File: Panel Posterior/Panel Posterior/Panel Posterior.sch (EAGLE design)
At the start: 1 part

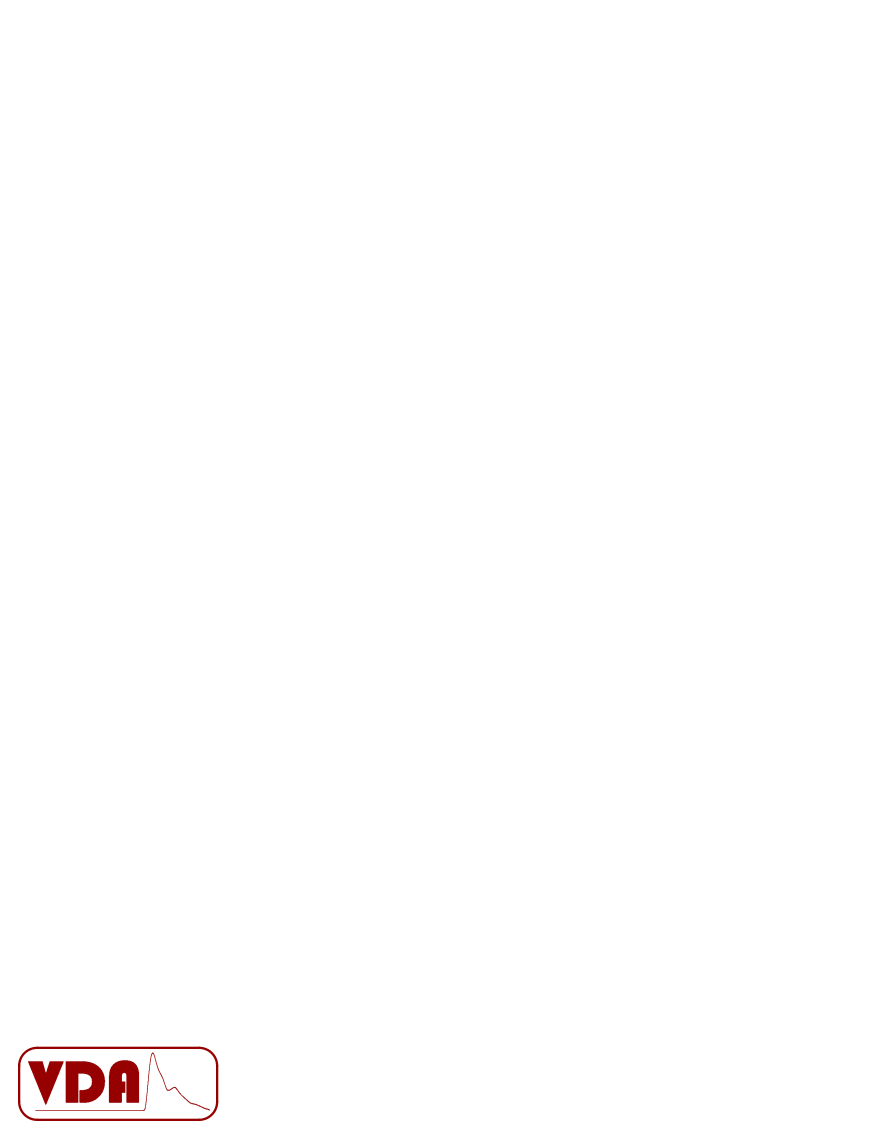
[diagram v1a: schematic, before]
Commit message: trabajando en los panelizados
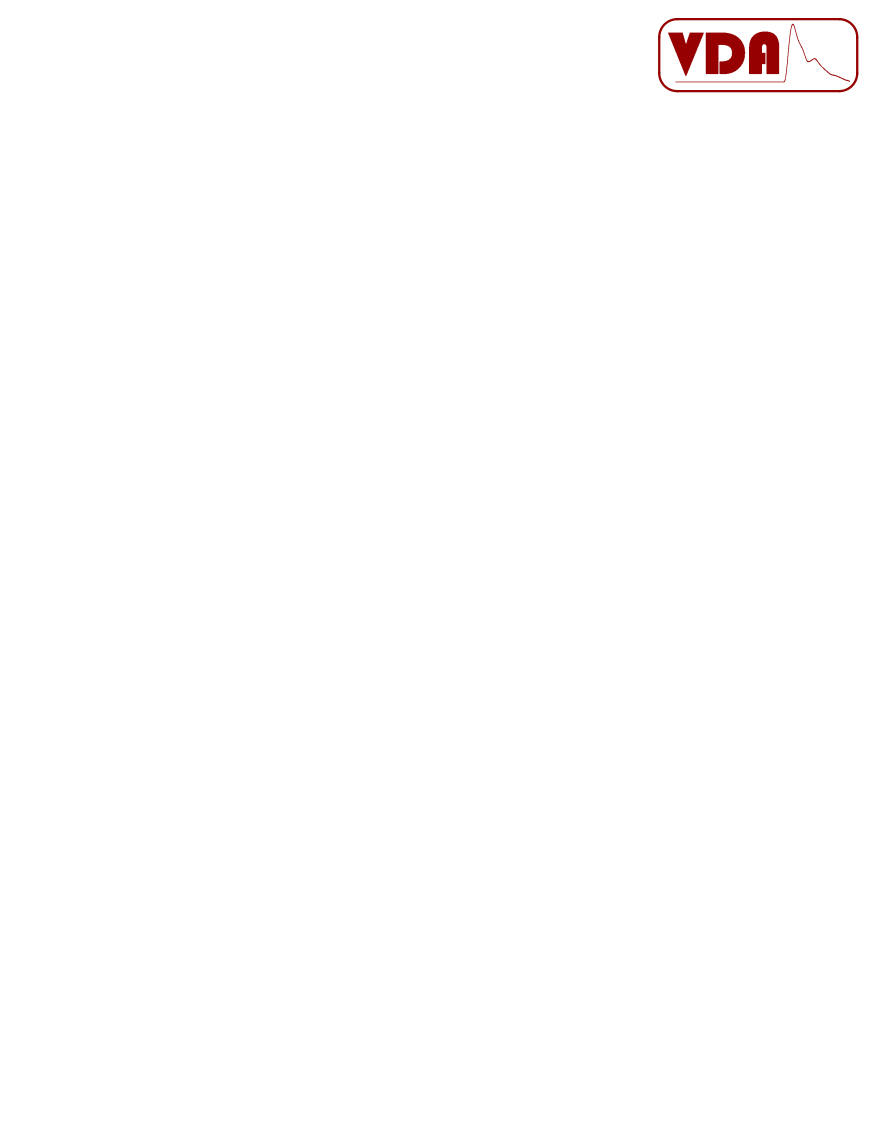
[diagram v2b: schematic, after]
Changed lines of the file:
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@@
 <attribute name="LAST_DATE_TIME" x="195.58" y="1.27" size="2.54" layer="97"/>
 </instance>
-<instance part="U$2" gate="G$1" x="45.72" y="5.08" smashed="yes"/>
+<instance part="U$2" gate="G$1" x="116.84" y="119.38" smashed="yes"/>
 </instances>
 <busses>
